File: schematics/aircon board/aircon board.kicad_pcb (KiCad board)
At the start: 2 copper layers, 19.1 x 33 mm, 10 parts, among them J1 CONN_04X2, J2 POWER_JACK, Q1 PN2222A, U1 VREG_3V3

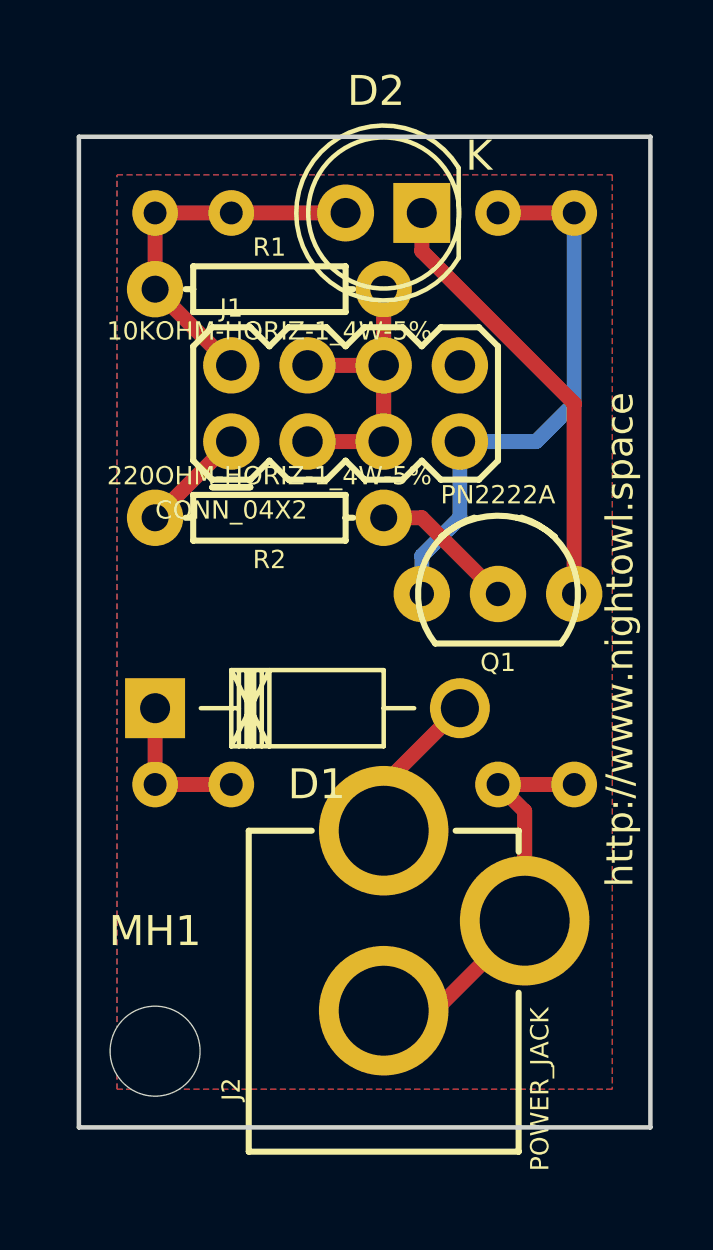
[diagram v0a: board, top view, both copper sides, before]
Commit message: Made vreg 3.3V component pads a little larger
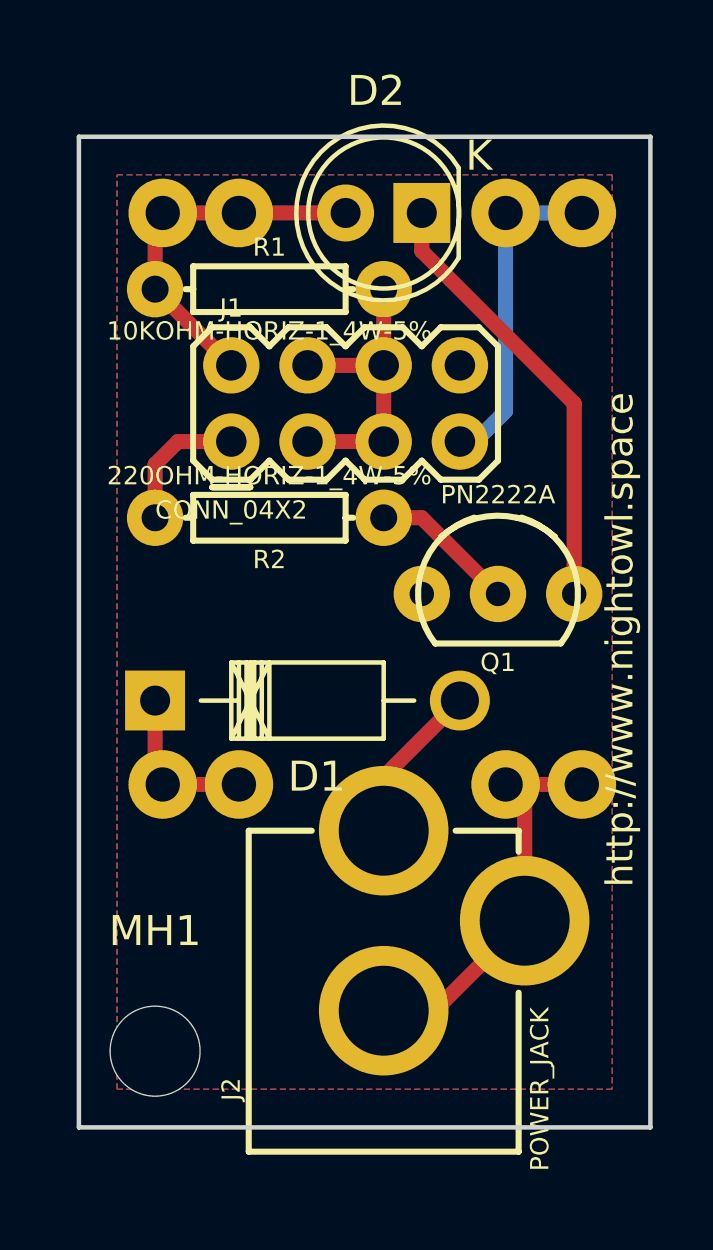
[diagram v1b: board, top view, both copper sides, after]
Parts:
- removed G***: LOGO, Nightowl logos:nightowl logo-faceonly
- moved D1 0.25 mm to (161.3, 84.8)
- moved U1 0.25 mm to (176.8, 67.3)
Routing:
- net GND: track 18.8 -> 11.1 mm
- net Net-(D1-Pad2): track 5.14 -> 6.93 mm
